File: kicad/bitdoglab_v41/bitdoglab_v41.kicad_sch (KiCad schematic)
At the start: 45 parts, among them J1 Conn_01x20_Socket, J10 GND, J11 GND, J12 Conn_01x05_Pin, J13 Conn_01x05_Pin, J14 5x5 Matrix led, J15 GND, J16 GND, J17 GND, J18 GND, J19 JOYSTICK, J2 conector_idc, J3 Conn_01x20_Socket, J4 jumper_mic, J5 Conn_01x05_Pin, J6 Conn_01x05_Pin, J7 GND, J8 GND, J9 GND, Q1 DMG2305UX-13, Q2 BC337, Q3 BC337, SW1 RESET, SW2 Button_A, SW3 Button_B, U1 3.3v_tht, U2 3.3v_smd, U3 BAT (DIS)CHARGE, U4 1063

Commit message: versao 4.1 diretamente no layout
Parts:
- removed U2: 3.3v_smd, Package_TO_SOT_SMD:SOT-223, symbol Regulator_Linear:uA7805
- added U2: LM1117DT-ADJ, Package_TO_SOT_SMD:TO-252-3_TabPin2, symbol Regulator_Linear:LM1117DT-ADJ
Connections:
- net +3.3V: now also U2.2 (VO)
- net GNDREF: now also U2.1 (ADJ)
- net VSYS: now also U2.3 (VI)

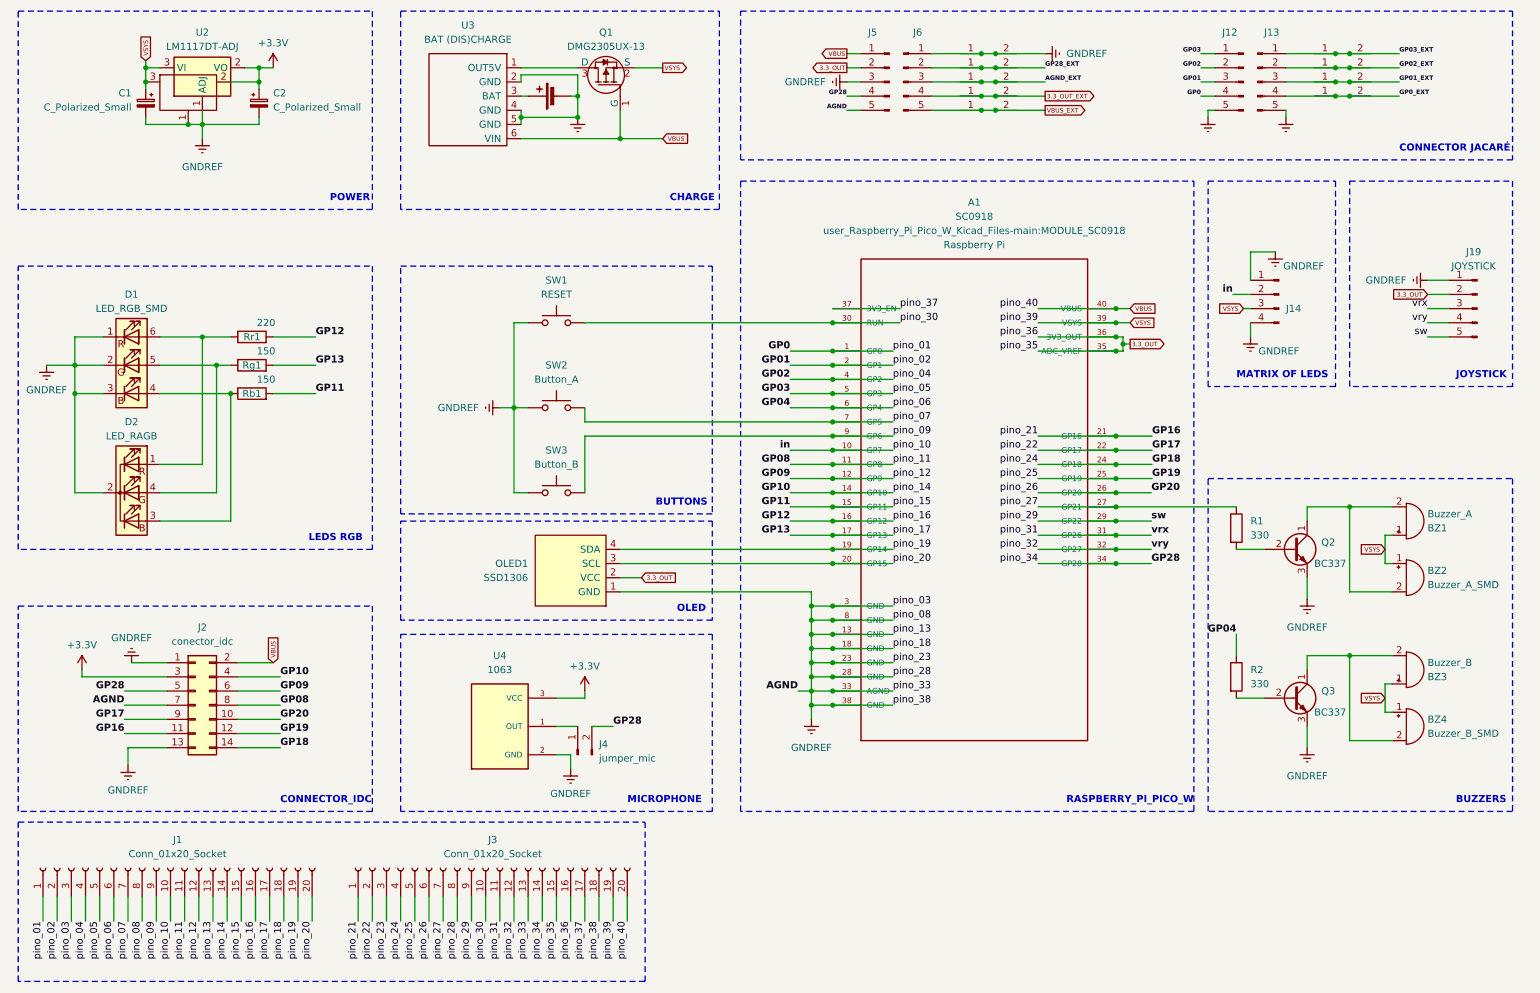
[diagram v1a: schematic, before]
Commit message: Mudar VBUS para VSYS no IDC e JACARE
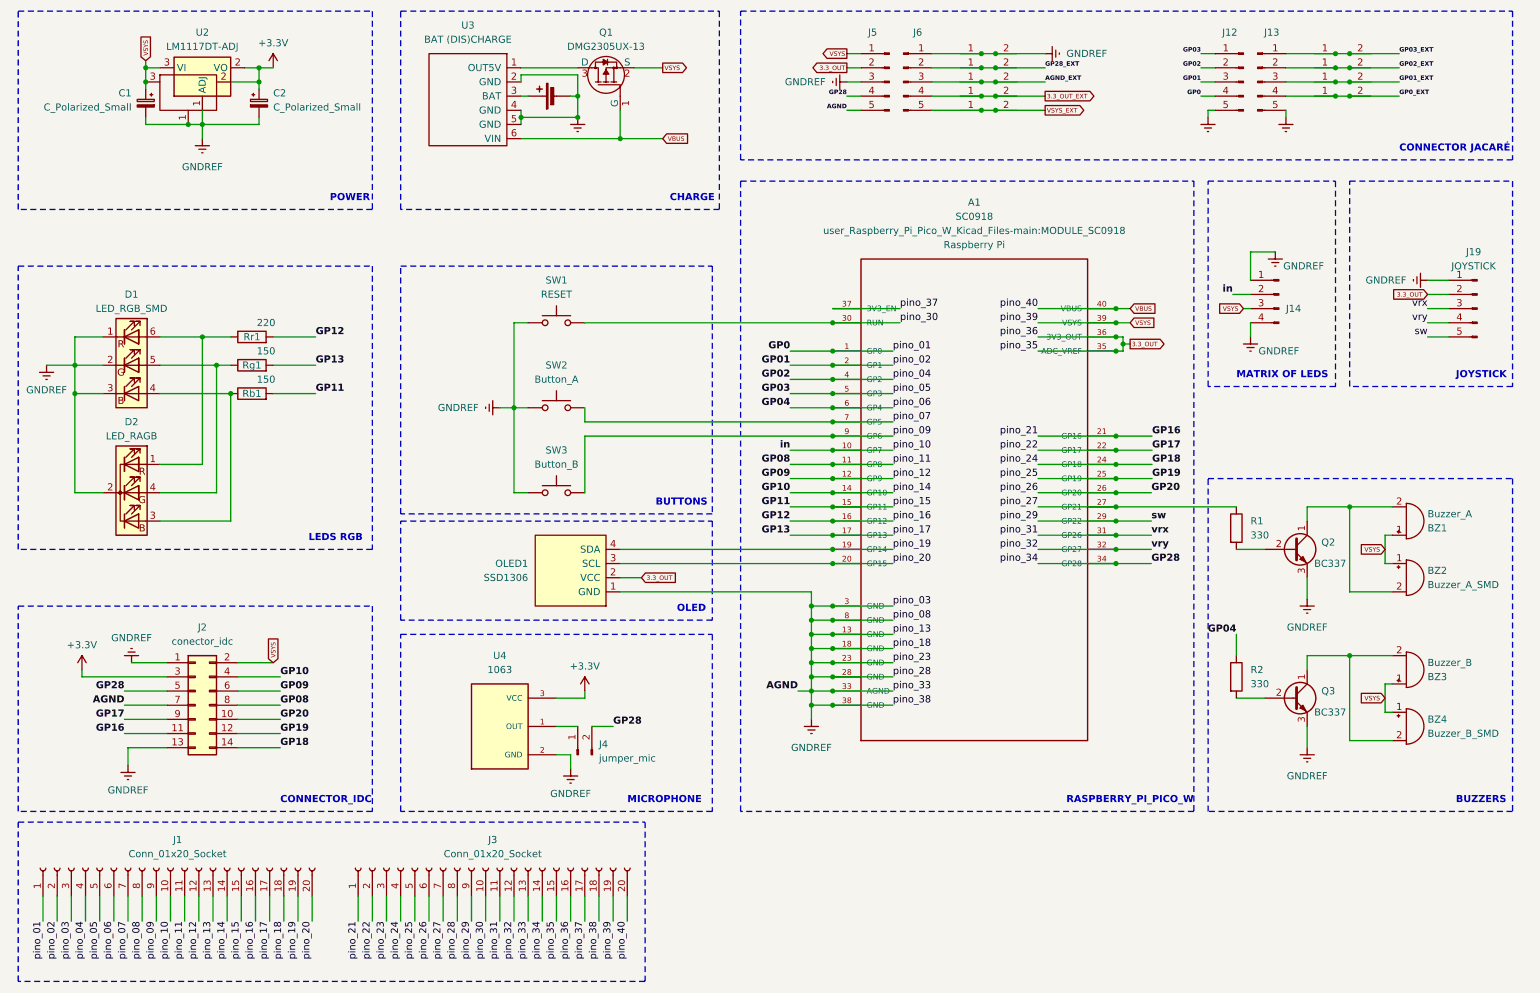
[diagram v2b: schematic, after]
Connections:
- net VBUS: no longer J2.2 (Pin_2), J5.1 (Pin_1)
- net VSYS: now also J2.2 (Pin_2), J5.1 (Pin_1)
- net VBUS_EXT renamed VSYS_EXT
